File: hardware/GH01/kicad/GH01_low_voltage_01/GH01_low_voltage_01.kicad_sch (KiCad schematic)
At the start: 10 parts, among them Q1 BS170, U1 XIAO ESP32C3

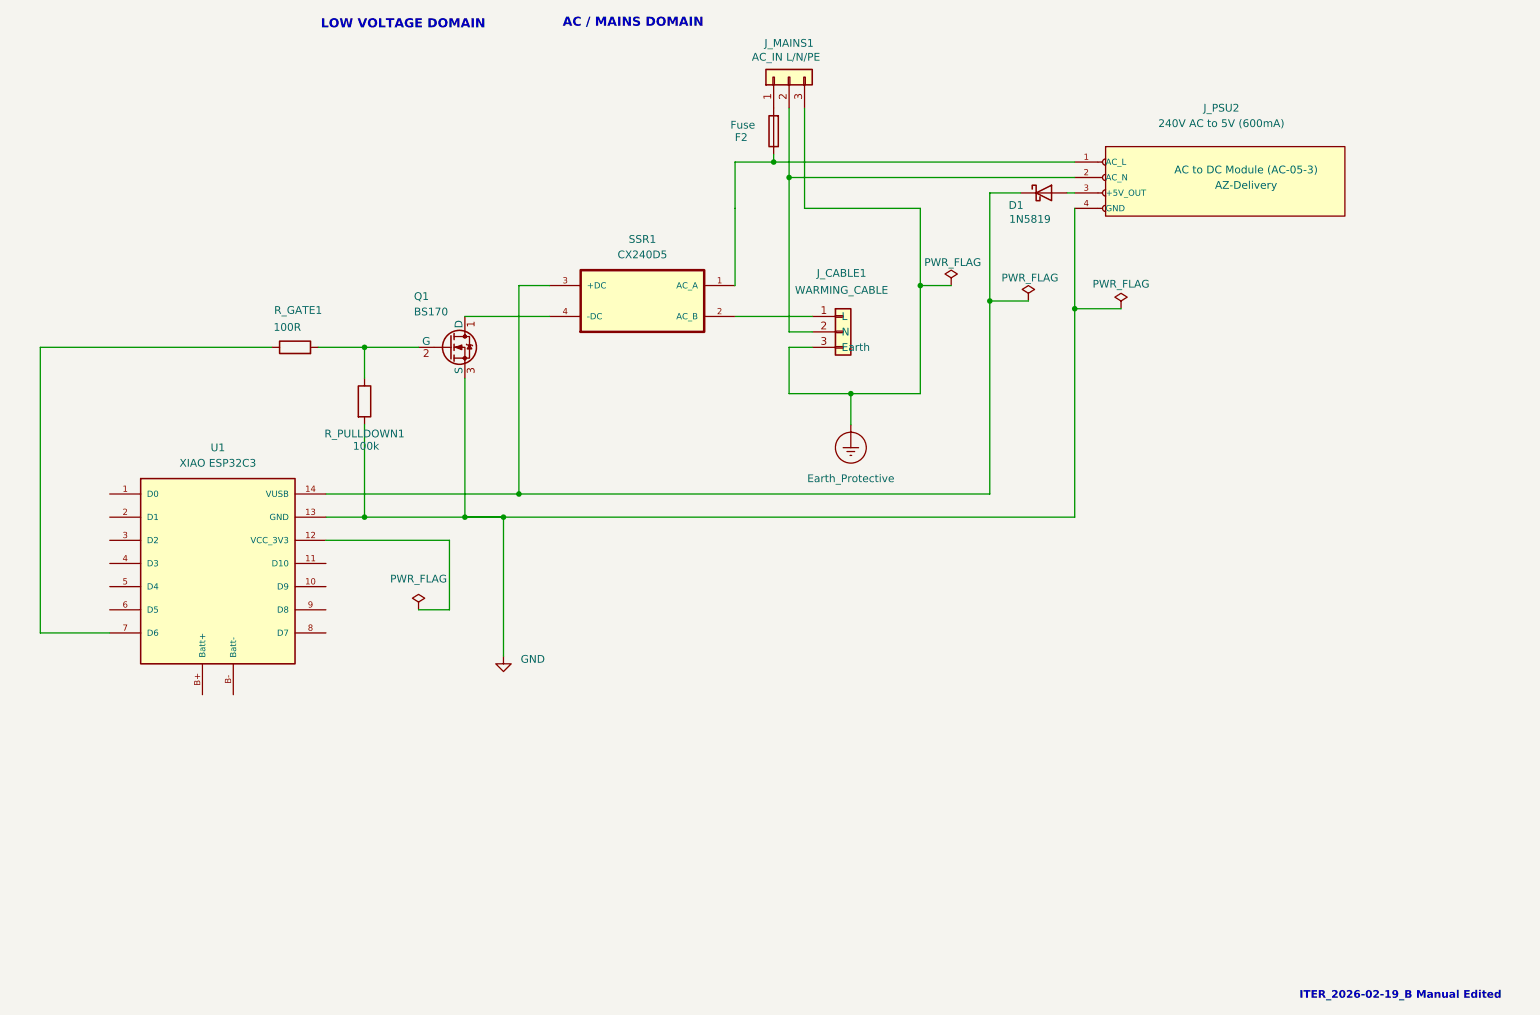
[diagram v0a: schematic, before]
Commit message: GH01: finalize LV schematic, test points, and spec alignment
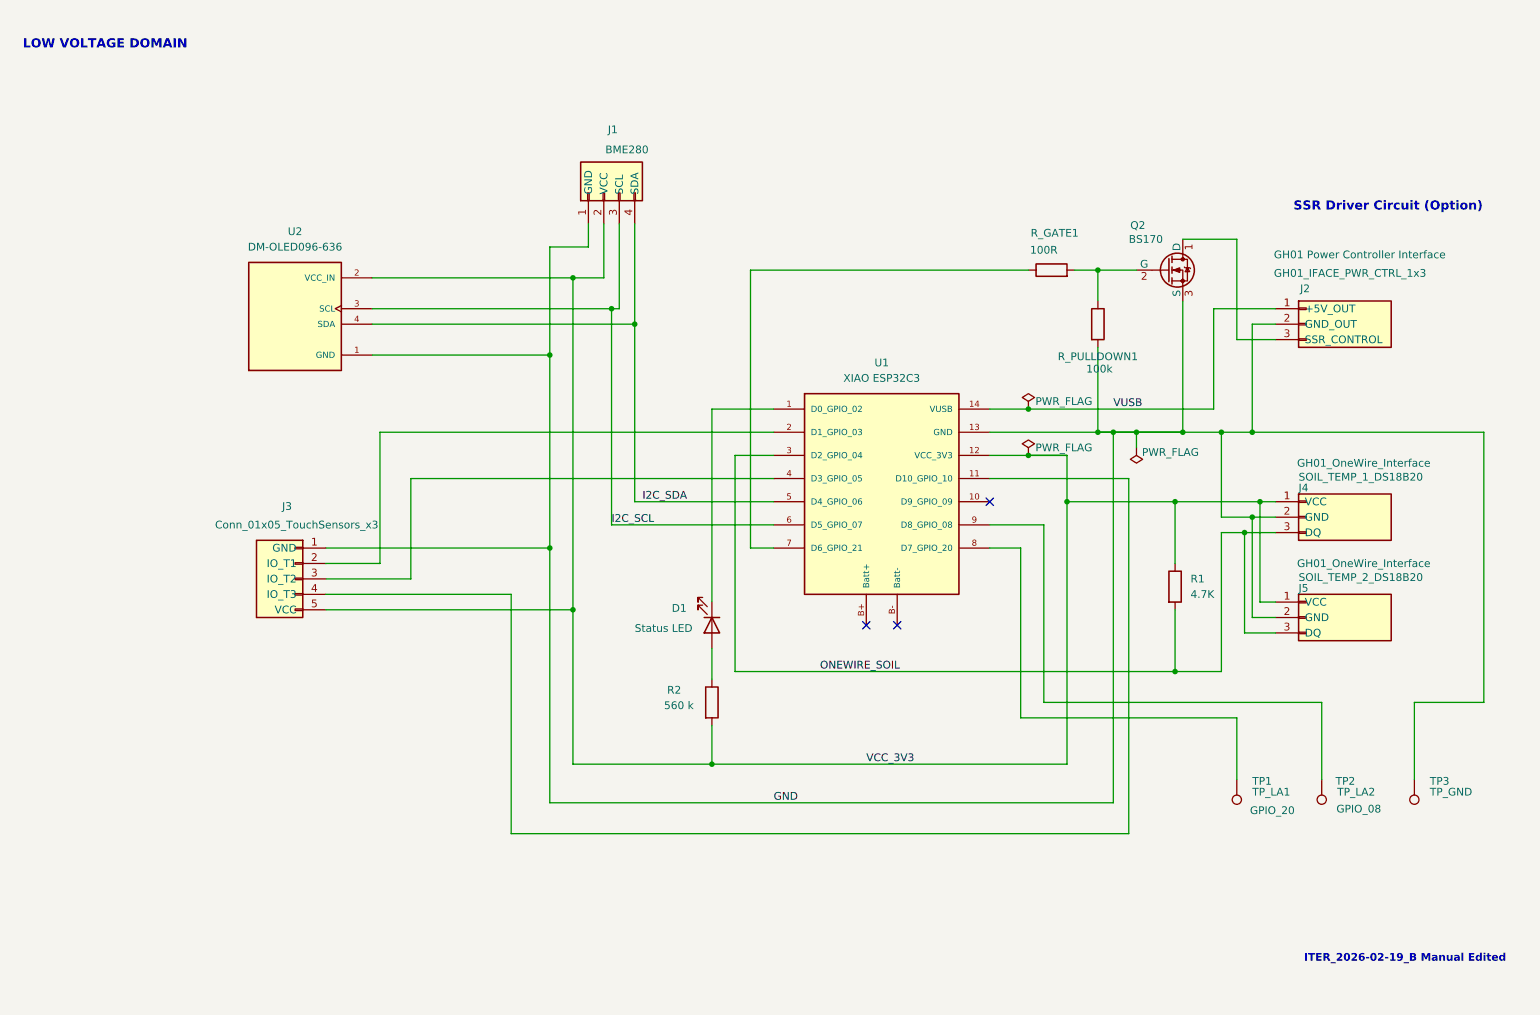
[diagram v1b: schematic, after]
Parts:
- removed D1: 1N5819, Diode_THT:D_DO-41_SOD81_P10.16mm_Horizontal, symbol Diode:1N5819
- removed F2: Fuse, symbol Device:Fuse
- removed J_CABLE1: WARMING_CABLE, symbol Connector_Generic:Conn_01x03
- removed J_MAINS1: AC_IN L/N/PE, symbol Connector_Generic:Conn_01x03
- removed J_PSU2: 240V AC to 5V (600mA), symbol AZ_Delivery:AC_to_5V_DC_Module
- removed Q1: BS170, Package_TO_SOT_THT:TO-92_Inline, symbol Transistor_FET:BS170
- removed SSR1: CX240D5, CX240D5:CRYDOM_CX240D5, symbol CX240D5:CX240D5
- added D1: Status LED, symbol Device:LED
- added J1: BME280, symbol GH01_custom:Conn_01x04_i2c
- added J2: GH01_IFACE_PWR_CTRL_1x3, symbol GH01_custom:GH01_IFACE_PWR_CTRL_1x3
- added J3: Conn_01x05_TouchSensors_x3, symbol GH01_custom:Conn_01x05_TouchSensors_x3
- added J4: SOIL_TEMP_1_DS18B20, symbol GH01_custom:GH01_OneWire_1x3
- added J5: SOIL_TEMP_2_DS18B20, symbol GH01_custom:GH01_OneWire_1x3
- added Q2: BS170, Package_TO_SOT_THT:TO-92_Inline, symbol GH01_custom:BS170
- added R1: 4.7K, symbol Device:R
- added R2: 560 k, symbol Device:R
- added TP1: TP_LA1, symbol Connector:TestPoint
- added TP2: TP_LA2, symbol Connector:TestPoint
- added TP3: TP_GND, symbol Connector:TestPoint
- added U2: DM-OLED096-636, DM-OLED096-636:MODULE_DM-OLED096-636, symbol DM-OLED096-636:DM-OLED096-636
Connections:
- net GND: now also J1.1 (GND), J2.2 (GND_OUT), J3.1 (GND), J4.2 (GND), J5.2 (GND), Q2.3 (S), TP3.1, U2.1 (GND)
- net VUSB: now reaches U1.14 (VUSB)
- net VUSB: now also J2.1 (+5V_OUT)
- net at R_GATE1.2, R_PULLDOWN1.1: now also Q2.2 (G)
- net at U1.1 (D0_GPIO_02): now also D1.1 (K)
- net at U1.11 (D10_GPIO_10): now also J3.4 (IO_T3)
- net VCC_3V3: now reaches U1.12 (VCC_3V3)
- net VCC_3V3: now also J1.2 (VCC), J3.5 (VCC), J4.1 (VCC), J5.1 (VCC), R1.1, R2.2, U2.2 (VCC_IN)
- net at U1.2 (D1_GPIO_03): now also J3.2 (IO_T1)
- net ONEWIRE_SOIL: now reaches U1.3 (D2_GPIO_04)
- net ONEWIRE_SOIL: now also J4.3 (DQ), J5.3 (DQ), R1.2
- net at U1.4 (D3_GPIO_05): now also J3.3 (IO_T2)
- net I2C_SDA: now reaches U1.5 (D4_GPIO_06)
- net I2C_SDA: now also J1.4 (SDA), U2.4 (SDA)
- net I2C_SCL: now reaches U1.6 (D5_GPIO_07)
- net I2C_SCL: now also J1.3 (SCL), U2.3 (SCL)
- net at U1.8 (D7_GPIO_20): now also TP1.1
- net at U1.9 (D8_GPIO_08): now also TP2.1
- new net: D1.2 (A), R2.1
- new net: J2.3 (SSR_CONTROL), Q2.1 (D)
- no-connect marks 0 -> 3
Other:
- note added: "SSR Driver Circuit (Option)"
- note removed: "AC / MAINS DOMAIN"
- title: GH01 Heater Control -> GH01 Heater Control - Low Voltage
- moved on the sheet: R_GATE1, R_PULLDOWN1, U1
